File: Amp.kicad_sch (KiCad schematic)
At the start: 1 part, among them U5 TPA3255DDVR

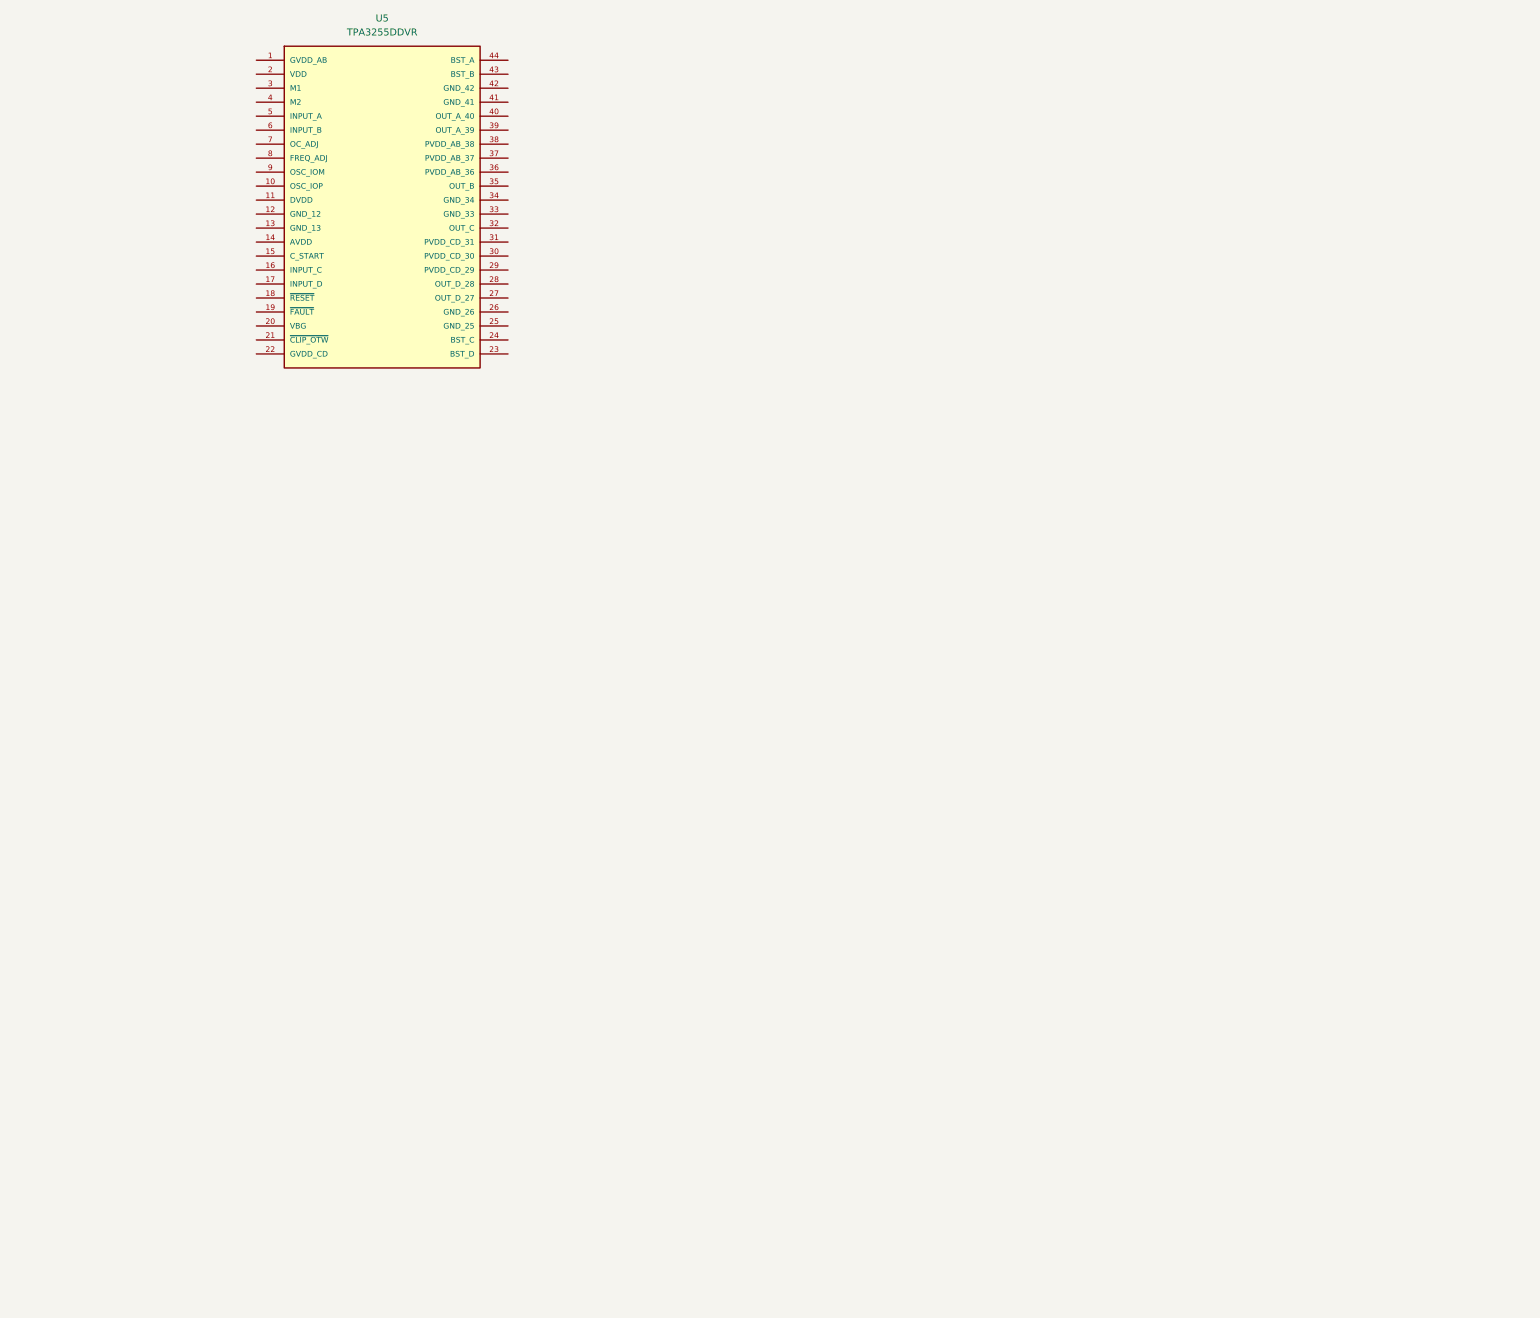
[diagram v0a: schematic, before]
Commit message: added first 2 amps
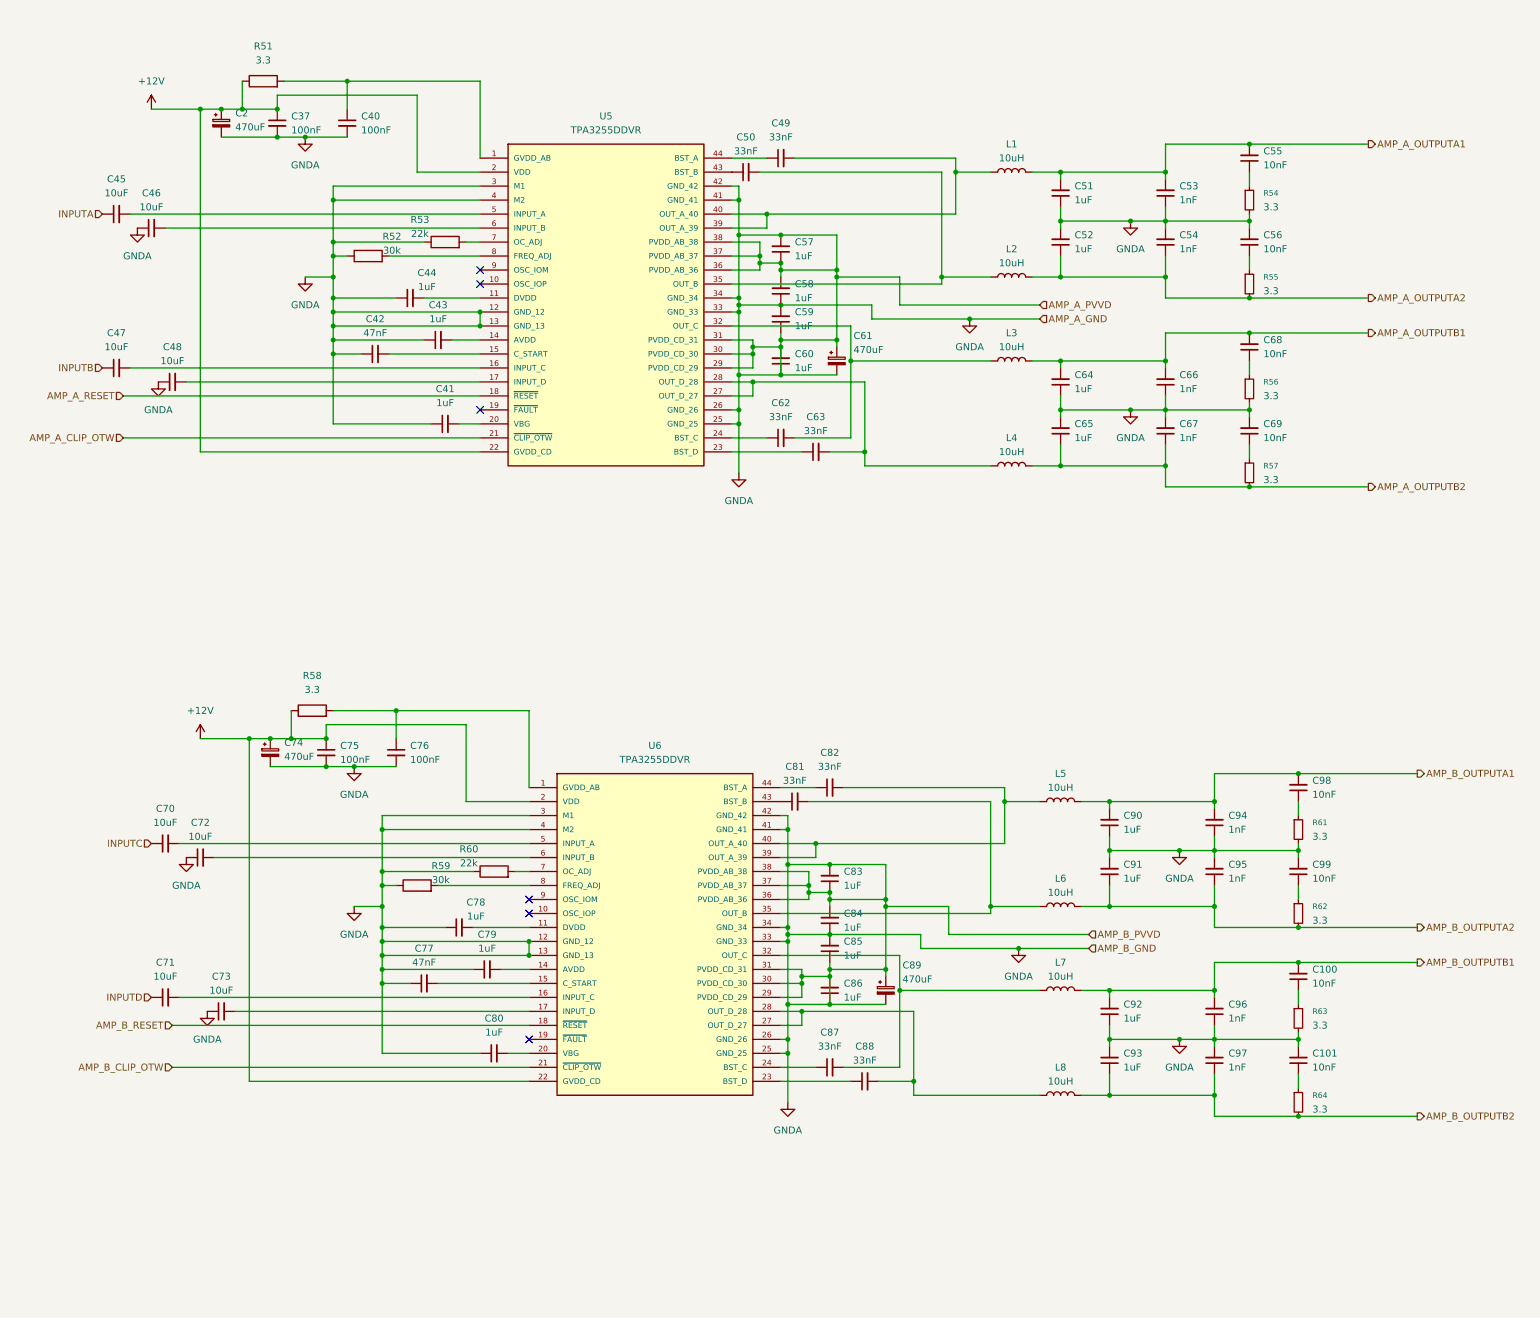
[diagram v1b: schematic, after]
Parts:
- added C100, C101, C55, C56, C68, C69, C98, C99: 10nF, symbol Device:C_Small
- added C2, C61, C74, C89: 470uF, symbol Device:C_Polarized_Small
- added C37, C40, C75, C76: 100nF, symbol Device:C_Small
- added C41, C43, C44, C51, C52, C57, C58, C59, C60, C64, C65, C78, C79, C80, C83, C84, C85, C86, C90, C91, C92, C93: 1uF, symbol Device:C_Small
- added C42, C77: 47nF, symbol Device:C_Small
- added C45, C46, C47, C48, C70, C71, C72, C73: 10uF, symbol Device:C_Small
- added C49, C50, C62, C63, C81, C82, C87, C88: 33nF, symbol Device:C_Small
- added C53, C54, C66, C67, C94, C95, C96, C97: 1nF, symbol Device:C_Small
- added L1, L2, L3, L4, L5, L6, L7, L8: 10uH, symbol Device:L
- added R51, R58: 3.3, symbol Device:R
- added R52, R59: 30k, symbol Device:R
- added R53, R60: 22k, symbol Device:R
- added R54, R55, R56, R57, R61, R62, R63, R64: 3.3, symbol Device:R_Small
- added U6: TPA3255DDVR, G-MuzikBox:SOP63P810X120-44N, symbol TPA3255DDVR:TPA3255DDVR
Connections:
- net at U5.1 (GVDD_AB): now also C40.1, R51.2
- net at U5.11 (DVDD): now also C44.2
- net GNDA: now reaches U5.12 (GND_12)
- net GNDA: now also U5.13 (GND_13), U5.25 (GND_25), U5.26 (GND_26), U5.29 (PVDD_CD_29), U5.3 (M1), U5.30 (PVDD_CD_30), U5.31 (PVDD_CD_31), U5.33 (GND_33), U5.34 (GND_34), U5.36 (PVDD_AB_36), U5.37 (PVDD_AB_37), U5.38 (PVDD_AB_38), U5.4 (M2), U5.41 (GND_41), U5.42 (GND_42), C101.2, C2.2, C37.2, C40.2, C41.1, C42.1, C43.1, C44.1, C46.1, C48.1, C51.1, C52.2, C53.1, C54.2, C56.2, C57.1, C57.2, C58.1, C58.2, C59.1, C59.2, C60.1, C60.2, C61.1, C61.2, C64.1, C65.2, C66.1, C67.2, C69.2, C72.1, C73.1, C74.2, C75.2, C76.2, C77.1, C78.1, C79.1, C80.1, C83.1, C83.2, C84.1, C84.2, C85.1, C85.2, C86.1, C86.2, C89.1, C89.2, C90.1, C91.2, C92.1, C93.2, C94.1, C95.2, C96.1, C97.2, C99.2, R52.1, R53.1, R54.2, R56.2, R59.1, R60.1, R61.2, R63.2, U6.12 (GND_12), U6.13 (GND_13), U6.25 (GND_25), U6.26 (GND_26), U6.29 (PVDD_CD_29), U6.3 (M1), U6.30 (PVDD_CD_30), U6.31 (PVDD_CD_31), U6.33 (GND_33), U6.34 (GND_34), U6.36 (PVDD_AB_36), U6.37 (PVDD_AB_37), U6.38 (PVDD_AB_38), U6.4 (M2), U6.41 (GND_41), U6.42 (GND_42)
- net at U5.14 (AVDD): now also C43.2
- net at U5.15 (C_START): now also C42.2
- net at U5.16 (INPUT_C): now also C47.2
- net at U5.17 (INPUT_D): now also C48.2
- net AMP_A_RESET: now reaches U5.18 (~{RESET})
- net +12V: now reaches U5.2 (VDD)
- net +12V: now also U5.22 (GVDD_CD), C2.1, C37.1, C74.1, C75.1, R51.1, R58.1, U6.2 (VDD), U6.22 (GVDD_CD)
- net at U5.20 (VBG): now also C41.2
- net AMP_A_CLIP_OTW: now reaches U5.21 (~{CLIP_OTW})
- net at U5.23 (BST_D): now also C63.1
- net at U5.24 (BST_C): now also C62.1
- net at U5.27 (OUT_D_27): now also U5.28 (OUT_D_28), C63.2, L4.1
- net at U5.32 (OUT_C): now also C62.2, L3.1
- net at U5.35 (OUT_B): now also C50.2, L2.1
- net at U5.39 (OUT_A_39): now also U5.40 (OUT_A_40), C49.2, L1.1
- net at U5.43 (BST_B): now also C50.1
- net at U5.44 (BST_A): now also C49.1
- net at U5.5 (INPUT_A): now also C45.2
- net at U5.6 (INPUT_B): now also C46.2
- net at U5.7 (OC_ADJ): now also R53.2
- net at U5.8 (FREQ_ADJ): now also R52.2
- new net: C78.2, U6.11 (DVDD)
- new net: C77.2, U6.15 (C_START)
- new net: C68.1, R56.1
- new net: C55.1, R54.1
- new net: C101.1, R64.1
- new net: C100.1, R63.1
- new net: C88.2, L8.1, U6.27 (OUT_D_27), U6.28 (OUT_D_28)
- new net: C82.1, U6.44 (BST_A)
- new net: C82.2, L5.1, U6.39 (OUT_A_39), U6.40 (OUT_A_40)
- new net: C69.1, R57.1
- new net: C98.1, R61.1
- new net: C88.1, U6.23 (BST_D)
- new net: C70.2, U6.5 (INPUT_A)
- new net: C56.1, R55.1
- new net: R60.2, U6.7 (OC_ADJ)
- new net: C81.1, U6.43 (BST_B)
- new net: C81.2, L6.1, U6.35 (OUT_B)
- new net: R59.2, U6.8 (FREQ_ADJ)
- new net: C72.2, U6.6 (INPUT_B)
- new net: C71.2, U6.16 (INPUT_C)
- new net: C87.1, U6.24 (BST_C)
- new net: C87.2, L7.1, U6.32 (OUT_C)
- new net: C76.1, R58.2, U6.1 (GVDD_AB)
- new net: C73.2, U6.17 (INPUT_D)
- new net: C99.1, R62.1
- new net: C80.2, U6.20 (VBG)
- new net: C79.2, U6.14 (AVDD)
- new net AMP_A_OUTPUTA1: C51.2, C53.2, C55.2, L1.2
- new net AMP_A_OUTPUTA2: C52.1, C54.1, L2.2, R55.2
- new net AMP_A_OUTPUTB1: C64.2, C66.2, C68.2, L3.2
- new net AMP_A_OUTPUTB2: C65.1, C67.1, L4.2, R57.2
- new net AMP_B_CLIP_OTW: U6.21 (~{CLIP_OTW})
- new net AMP_B_OUTPUTA1: C90.2, C94.2, C98.2, L5.2
- new net AMP_B_OUTPUTA2: C91.1, C95.1, L6.2, R62.2
- new net AMP_B_OUTPUTB1: C100.2, C92.2, C96.2, L7.2
- new net AMP_B_OUTPUTB2: C93.1, C97.1, L8.2, R64.2
- new net AMP_B_RESET: U6.18 (~{RESET})
- new net INPUTA: C45.1
- new net INPUTB: C47.1
- new net INPUTC: C70.1
- new net INPUTD: C71.1
- no-connect marks 0 -> 6
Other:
- moved on the sheet: U5

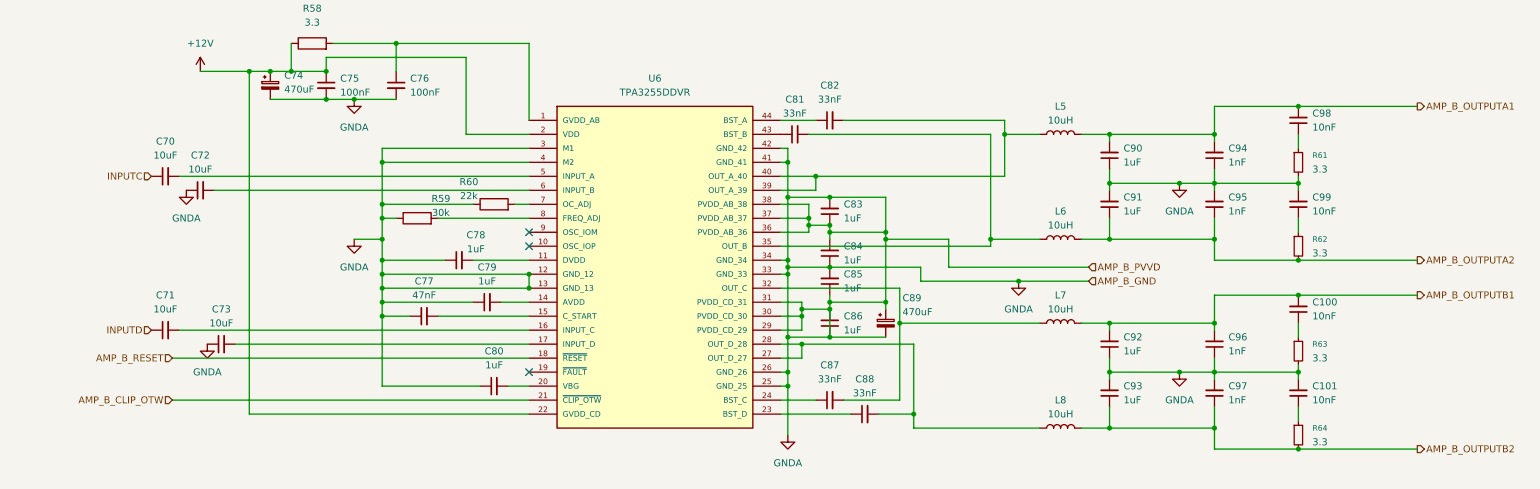
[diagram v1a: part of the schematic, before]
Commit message: adjusted mono amp for center speaker
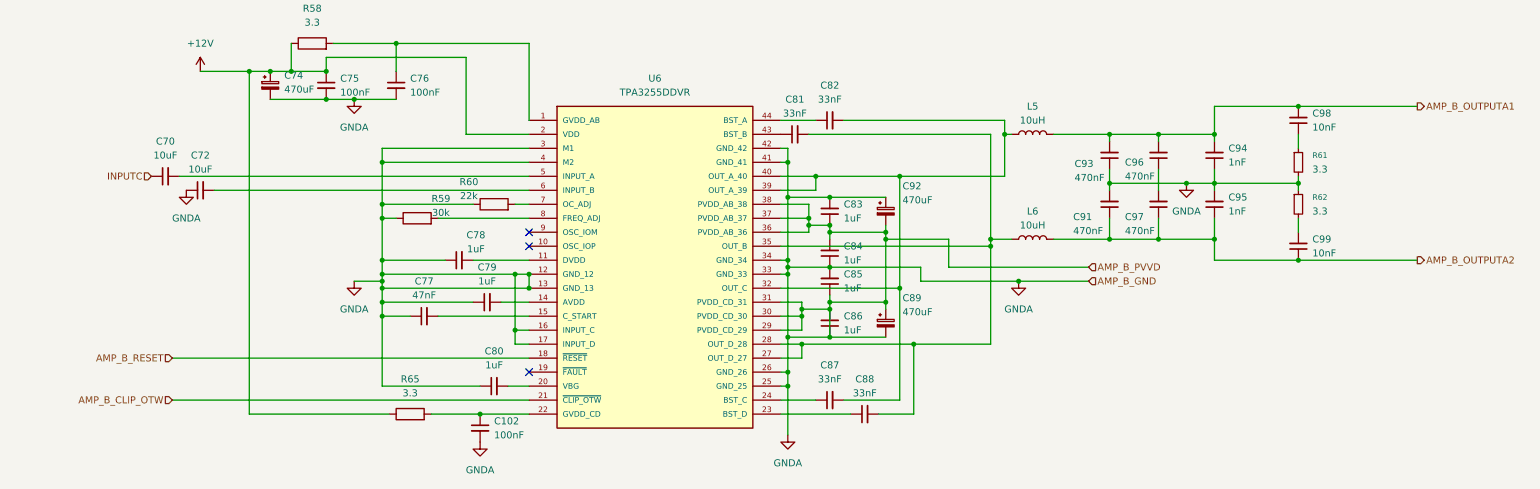
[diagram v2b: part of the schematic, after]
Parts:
- removed C100, C101: 10nF, symbol Device:C_Small
- removed C71, C73: 10uF, symbol Device:C_Small
- removed C90, C92: 1uF, symbol Device:C_Small
- removed L7, L8: 10uH, symbol Device:L
- removed R63, R64: 3.3, symbol Device:R_Small
- added C102: 100nF, symbol Device:C_Small
- added C92: 470uF, symbol Device:C_Polarized_Small
- added R65: 3.3, symbol Device:R
- C91, C93: value 1uF -> 470nF
- C96, C97: value 1nF -> 470nF
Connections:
- net AMP_B_OUTPUTB1 is gone; now on net AMP_B_OUTPUTA1: C96.2
- net +12V: now also R65.1; no longer U6.22 (GVDD_CD)
- net AMP_B_OUTPUTA1: now also C93.2
- net AMP_B_OUTPUTA2: now also C97.1, C99.1; no longer R62.2
- net GNDA: now also C93.1, R62.1, U6.16 (INPUT_C), U6.17 (INPUT_D), C102.2, C92.1, C92.2; no longer C93.2, C96.1, C97.2, C99.2
- net at C88.2, U6.27 (OUT_D_27), U6.28 (OUT_D_28): now also C81.2, L6.1, U6.35 (OUT_B)
- net at C82.2, L5.1, U6.39 (OUT_A_39)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: now also C87.2, U6.32 (OUT_C)
- removed net AMP_B_OUTPUTB2: C93.1, C97.1
- new net: C96.1, C97.2
- new net: C102.1, R65.2, U6.22 (GVDD_CD)
- new net: C99.2, R62.2
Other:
- moved on the sheet: C99, L5, L6, R62

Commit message: this is going to be mad expensive
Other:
- note added: "+12V should be a separate rail."
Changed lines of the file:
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@@
 	(generator_version "10.0")
 	(paper "A3")
+	(text "+12V should be a separate rail."
+		(exclude_from_sim no)
+		(at 143.764 245.364 0)
+		(effects
+			(font
+				(size 5.08 5.08)
+			)
+		)
+	)
 	(junction
 		(at 173.99 189.23)
